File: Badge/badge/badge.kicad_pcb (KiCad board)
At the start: 2 copper layers, 50 x 50 mm, 12 parts, among them J1 USB_B_Micro, J2 Conn_01x05, U1 FT232RL

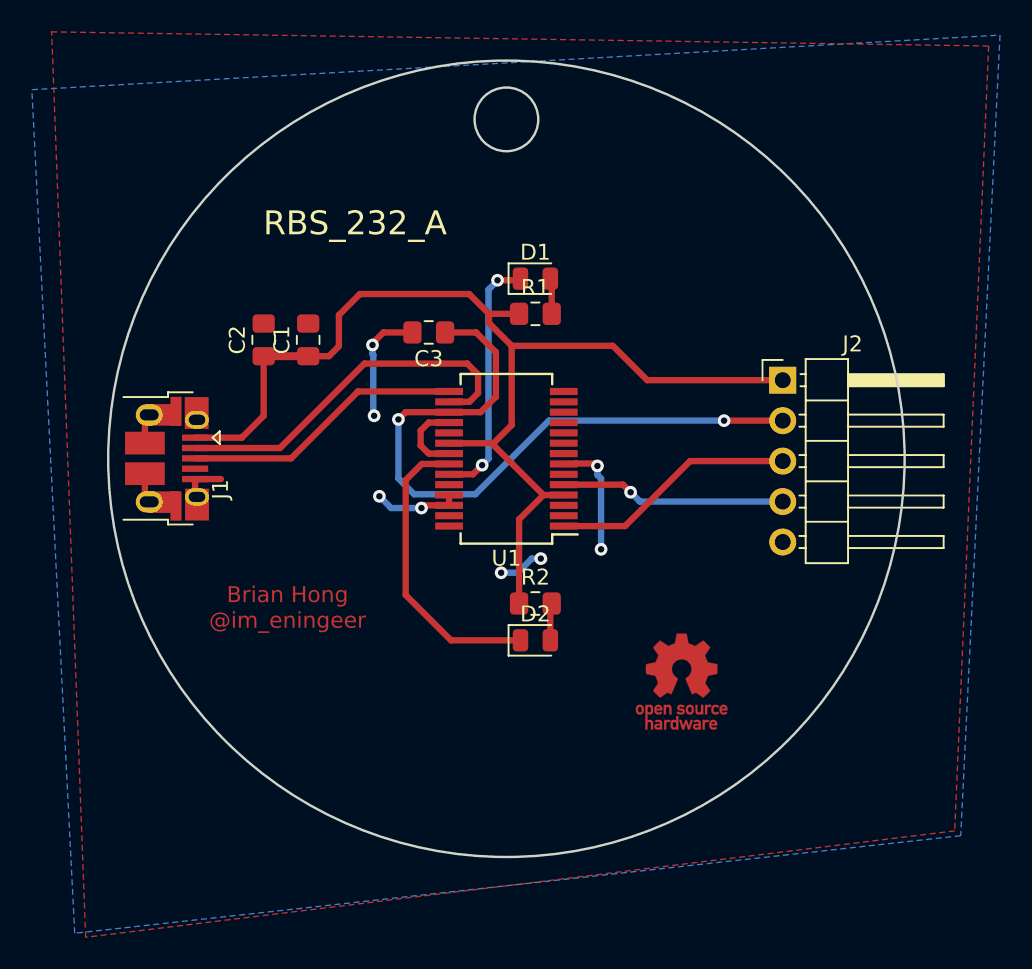
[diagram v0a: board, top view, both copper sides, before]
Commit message: Fixed and panelized
Added text to RS232 board
Added on/off switch to main board
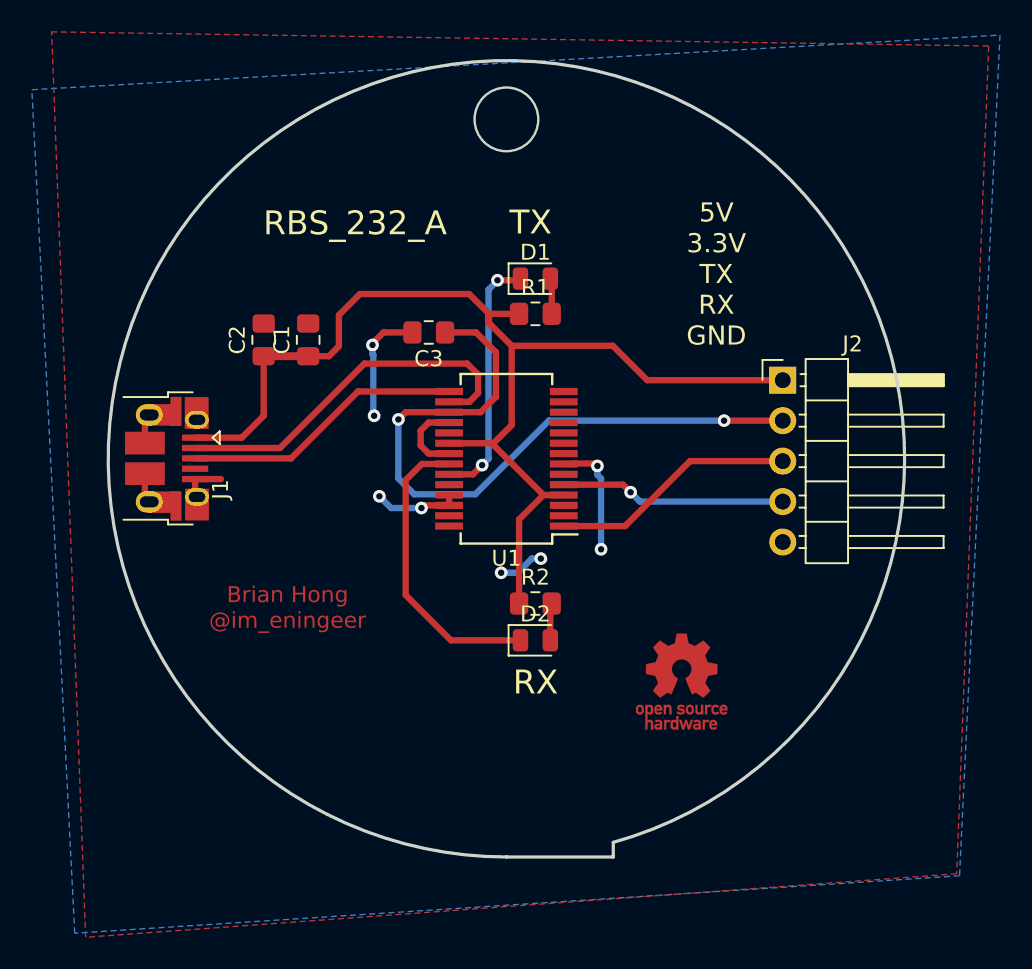
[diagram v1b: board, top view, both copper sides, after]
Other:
- outline, holes or cut-outs redrawn
- board text added: "5V 3.3V TX RX GND"
- board text added: "RX"
- board text added: "TX"
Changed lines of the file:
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@@
   (general
     (thickness 1.6)
-    (drawings 4)
+    (drawings 9)
     (tracks 120)
     (zones 0)
@@
     (trace_min 0.2)
     (segment_width 0.2)
-    (edge_width 0.15)
+    (edge_width 0.2)
     (via_size 0.8)
     (via_drill 0.4)
@@
       (xy -1.971615 1.454739) (xy -1.908759 1.469184)) (layer F.Cu) (width 0.01))
   )
+  (gr_text RX (at 170.8404 107.8484) (layer F.SilkS)
+    (effects (font (size 1.5 1.5) (thickness 0.3)))
+  )
+  (gr_text TX (at 170.5356 78.9686) (layer F.SilkS)
+    (effects (font (size 1.5 1.5) (thickness 0.3)))
+  )
+  (gr_text "5V\n3.3V\nTX\nRX\nGND" (at 182.1942 82.2198) (layer F.SilkS)
+    (effects (font (size 1.2 1.2) (thickness 0.2)))
+  )
+  (gr_line (start 175.720073 117.891714) (end 175.720073 118.806114) (layer Edge.Cuts) (width 0.2))
+  (gr_line (start 169.0116 118.8086) (end 175.7172 118.8086) (layer Edge.Cuts) (width 0.2))
+  (gr_arc (start 169.0116 93.8086) (end 169.0116 118.8086) (angle 344.434553) (layer Edge.Cuts) (width 0.2))
   (gr_circle (center 169.0116 72.5) (end 171.0116 72.5) (layer Edge.Cuts) (width 0.15))
   (gr_text "Brian Hong\n@im_eningeer" (at 155.2702 103.1494) (layer F.Cu)
@@
     (effects (font (size 1.5 1.5) (thickness 0.3)))
   )
-  (gr_circle (center 169.0116 93.8086) (end 194.0116 93.8086) (layer Edge.Cuts) (width 0.15))
   (segment (start 171.3992 100.1522) (end 171.2468 100.1522) (width 0.4) (layer F.Cu) (net 0))
   (via (at 171.1706 100.076) (size 0.8) (drill 0.4) (layers F.Cu B.Cu) (net 0))
@@
     (polygon
       (pts
-        (xy 140.4366 67.0052) (xy 199.2884 67.8942) (xy 197.1548 117.1702) (xy 142.5956 123.8504) (xy 140.462 67.0306)
+        (xy 140.4366 67.0052) (xy 199.2884 67.8942) (xy 197.2818 119.8626) (xy 142.5956 123.8504) (xy 140.462 67.0306)
       )
     )
@@
     (polygon
       (pts
-        (xy 139.2174 70.6374) (xy 199.9996 67.2084) (xy 197.5358 117.475) (xy 141.9098 123.5964)
+        (xy 139.2174 70.6374) (xy 199.9996 67.2084) (xy 197.4596 119.9896) (xy 141.9098 123.5964)
       )
     )

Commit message: Output (not sure what changed)
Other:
- outline, holes or cut-outs redrawn
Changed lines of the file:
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@@
   (general
     (thickness 1.6)
-    (drawings 9)
+    (drawings 8)
     (tracks 120)
     (zones 0)
@@
     (visible_elements FFFFFF7F)
     (pcbplotparams
-      (layerselection 0x010fc_ffffffff)
+      (layerselection 0x010f0_ffffffff)
       (usegerberextensions false)
       (usegerberattributes false)
@@
       (outputformat 1)
       (mirror false)
-      (drillshape 1)
+      (drillshape 0)
       (scaleselection 1)
-      (outputdirectory ""))
+      (outputdirectory "output"))
   )
   (net 0 "")
@@
       (xy -1.971615 1.454739) (xy -1.908759 1.469184)) (layer F.Cu) (width 0.01))
   )
+  (gr_circle (center 169.0116 93.8086) (end 192.5116 93.8086) (layer F.SilkS) (width 0.2))
+  (gr_circle (center 169.0116 93.8086) (end 194.0116 93.8086) (layer Edge.Cuts) (width 0.2))
   (gr_text RX (at 170.8404 107.8484) (layer F.SilkS)
     (effects (font (size 1.5 1.5) (thickness 0.3)))
@@
     (effects (font (size 1.2 1.2) (thickness 0.2)))
   )
-  (gr_line (start 175.720073 117.891714) (end 175.720073 118.806114) (layer Edge.Cuts) (width 0.2))
-  (gr_line (start 169.0116 118.8086) (end 175.7172 118.8086) (layer Edge.Cuts) (width 0.2))
-  (gr_arc (start 169.0116 93.8086) (end 169.0116 118.8086) (angle 344.434553) (layer Edge.Cuts) (width 0.2))
   (gr_circle (center 169.0116 72.5) (end 171.0116 72.5) (layer Edge.Cuts) (width 0.15))
   (gr_text "Brian Hong\n@im_eningeer" (at 155.2702 103.1494) (layer F.Cu)
